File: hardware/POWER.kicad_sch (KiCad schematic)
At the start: 67 parts, among them J4 532610371, SW1 TS-1010-C-A, U1 RT5750A, U13 XC6206P302MR, U2 RT9467, U3 RT4812, U5 RT6150, U6 RT5750A, U7 RT5750A

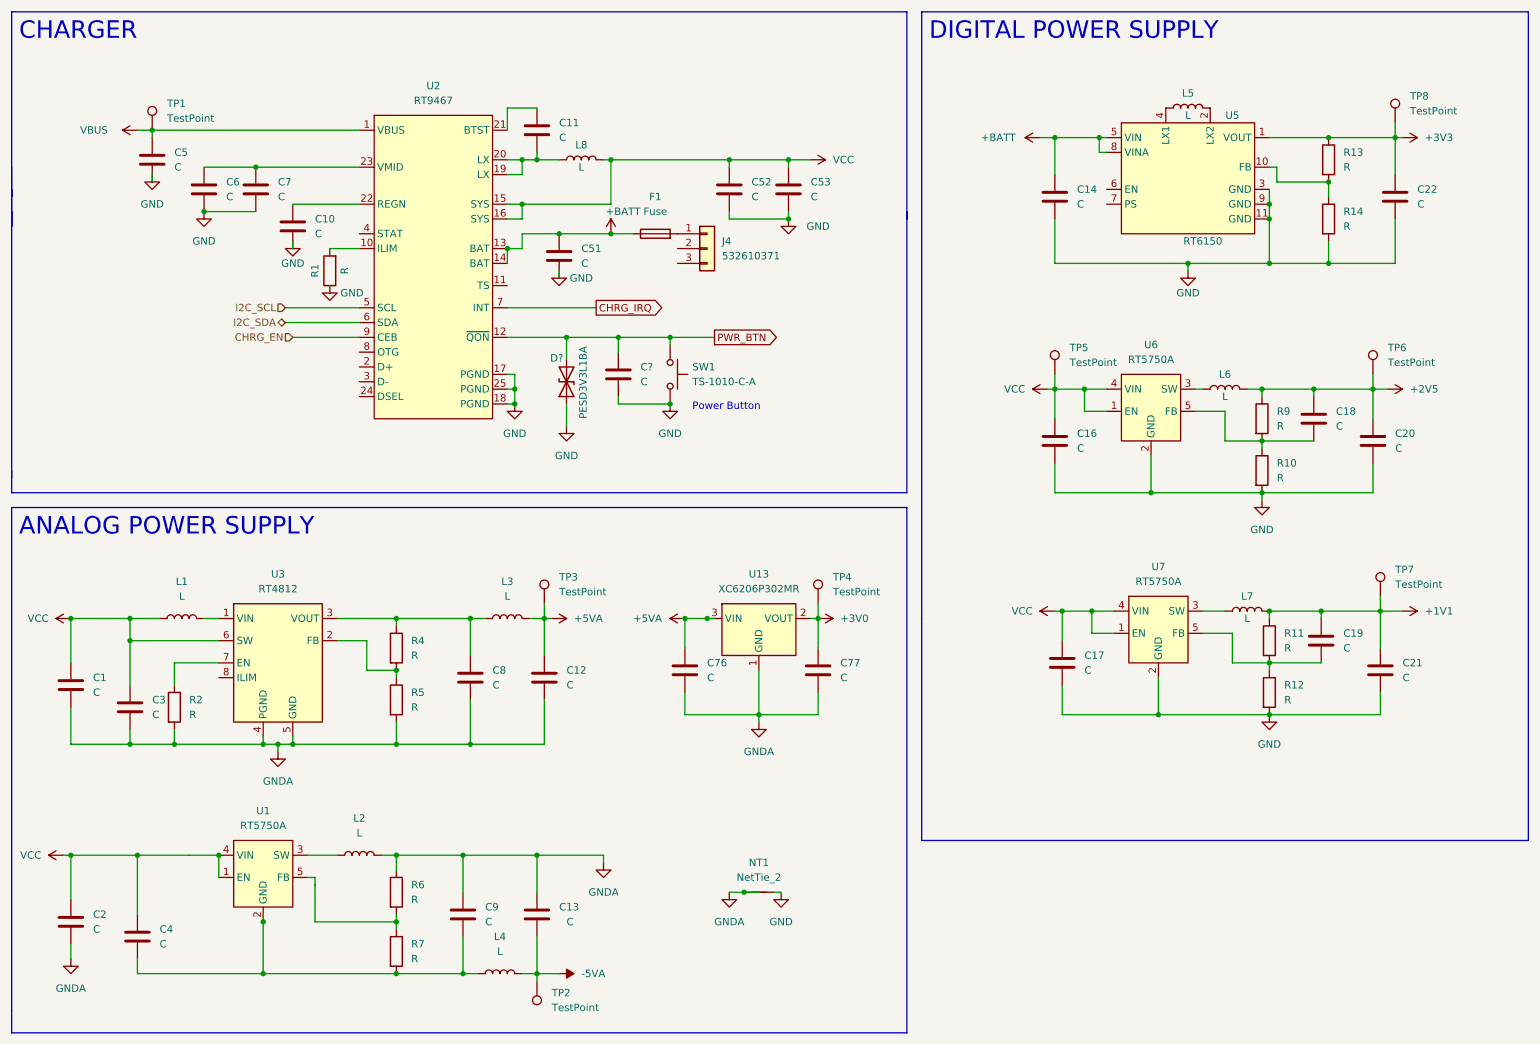
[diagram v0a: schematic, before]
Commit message: replaced dc-dc ics
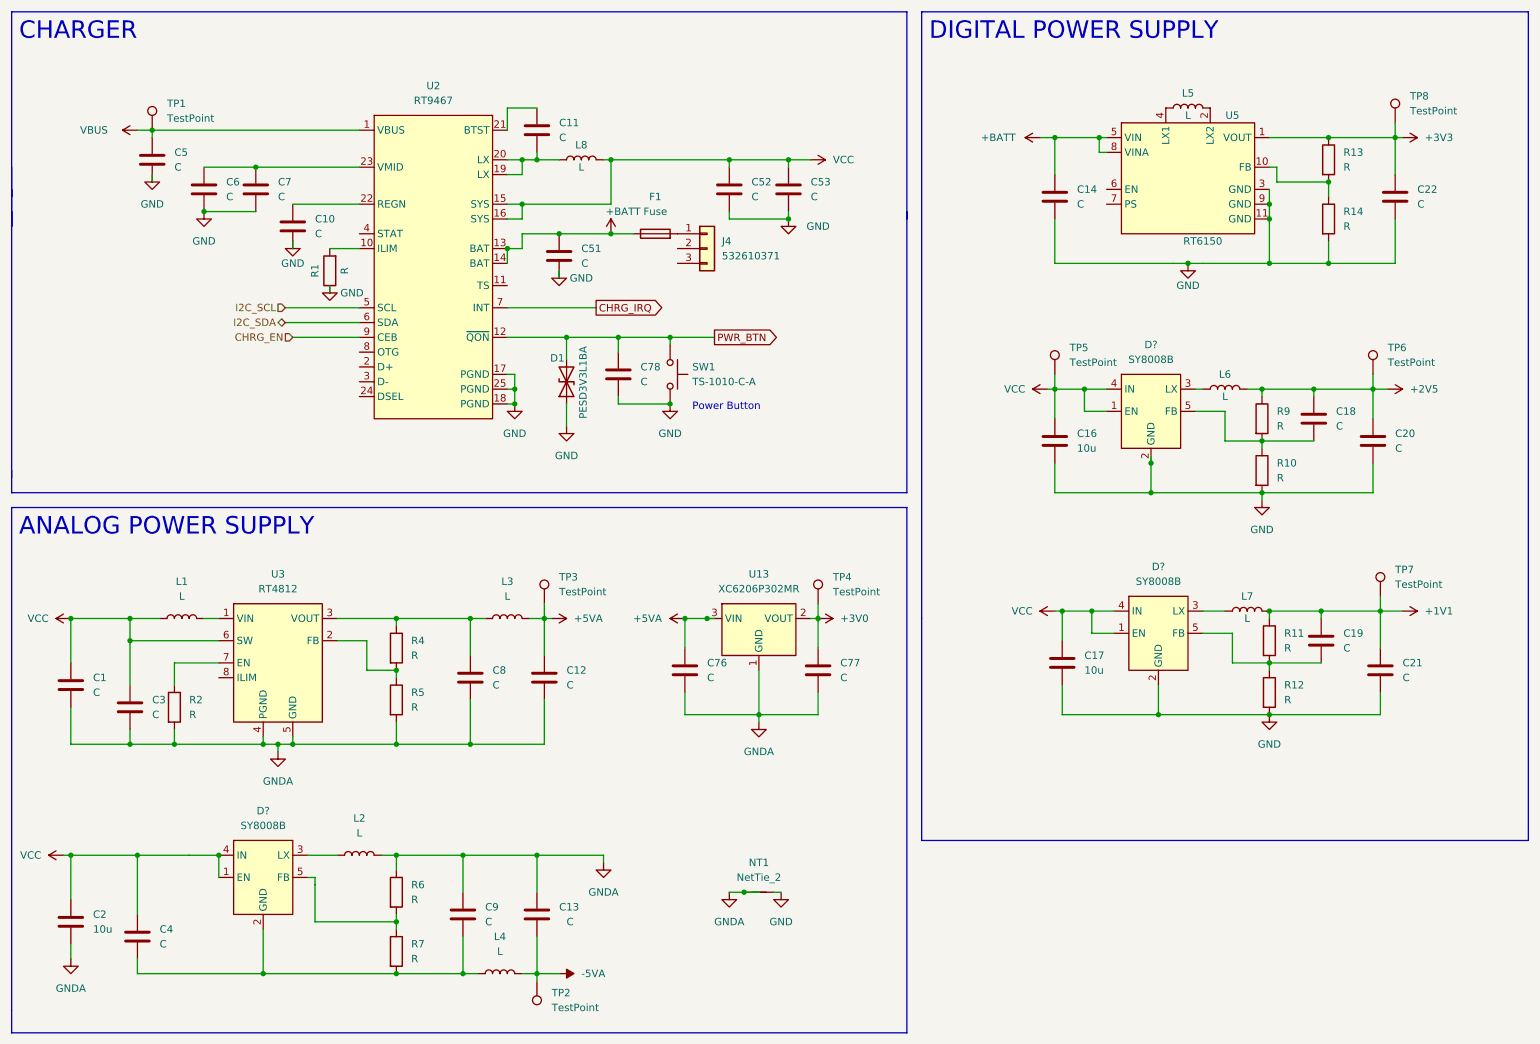
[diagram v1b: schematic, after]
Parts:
- removed U1, U6, U7: RT5750A, rlib_power:SOT-23-5, symbol rlib_power:RT5750A
- added D? (x3): SY8008B, rlib_power:SOT-23-5, symbol rlib_power:SY8008B
- C16, C17, C2: value C -> 10u
- gave numbers to parts that had none: 2
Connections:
- net GND: now also D?.2 (GND), D?.2 (GND)
- net VCC: now also D?.1 (EN), D?.1 (EN), D?.1 (EN), D?.4 (IN), D?.4 (IN), D?.4 (IN)
- net at L2.1: now also D?.3 (LX)
- net at R6.2, R7.1: now also D?.5 (FB)
- net at C4.2, C9.2, L4.1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: now also D?.2 (GND)
- net at C19.2, R11.2, R12.1: now also D?.5 (FB)
- net at L6.1: now also D?.3 (LX)
- net at C18.2, R10.1, R9.2: now also D?.5 (FB)
- net at L7.1: now also D?.3 (LX)

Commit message: sfsf
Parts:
- SW1: footprint rlib_buttons:TS-1010-X-X -> rlib_buttons:GT-TC054A-H035-L1; symbol rlib_buttons:TS-1010-C-A -> rlib_buttons:GT-TC054A-H035-L1
- gave numbers to parts that had none: 3
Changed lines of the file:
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@@
   (symbol (lib_id "rlib_power:SY8008B") (at 214.63 88.9 0) (unit 1)
     (in_bom yes) (on_board yes) (fields_autoplaced)
-    (property "Reference" "D?" (id 0) (at 214.63 77.47 0))
+    (property "Reference" "D12" (id 0) (at 214.63 77.47 0))
     (property "Value" "SY8008B" (id 1) (at 214.63 80.01 0))
     (property "Footprint" "rlib_power:SOT-23-5" (id 2) (at 226.06 81.28 0)
@@
   (symbol (lib_id "rlib_power:SY8008B") (at 215.9 127 0) (unit 1)
     (in_bom yes) (on_board yes) (fields_autoplaced)
-    (property "Reference" "D?" (id 0) (at 215.9 115.57 0))
+    (property "Reference" "D13" (id 0) (at 215.9 115.57 0))
     (property "Value" "SY8008B" (id 1) (at 215.9 118.11 0))
     (property "Footprint" "rlib_power:SOT-23-5" (id 2) (at 227.33 119.38 0)
@@
     (pin "1")
   )
-  (symbol (lib_id "rlib_buttons:TS-1010-C-A") (at 132.08 82.55 270) (unit 1)
+  (symbol (lib_id "rlib_buttons:GT-TC054A-H035-L1") (at 132.08 82.55 270) (unit 1)
     (in_bom yes) (on_board yes) (fields_autoplaced)
     (property "Reference" "SW1" (id 0) (at 135.89 81.2799 90)
@@
       (effects (font (size 1.27 1.27)) (justify left))
     )
-    (property "Footprint" "rlib_buttons:TS-1010-X-X" (id 2) (at 127 81.28 0)
+    (property "Footprint" "rlib_buttons:GT-TC054A-H035-L1" (id 2) (at 127 81.28 0)
       (effects (font (size 1.27 1.27)) hide)
     )
@@
   (symbol (lib_id "rlib_power:SY8008B") (at 62.23 168.91 0) (unit 1)
     (in_bom yes) (on_board yes) (fields_autoplaced)
-    (property "Reference" "D?" (id 0) (at 62.23 157.48 0))
+    (property "Reference" "D11" (id 0) (at 62.23 157.48 0))
     (property "Value" "SY8008B" (id 1) (at 62.23 160.02 0))
     (property "Footprint" "rlib_power:SOT-23-5" (id 2) (at 73.66 161.29 0)

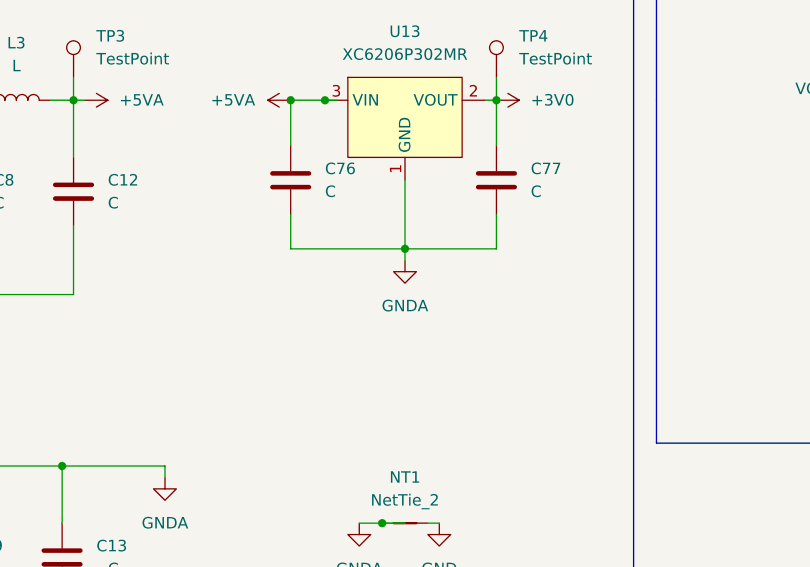
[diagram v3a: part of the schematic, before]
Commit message: added new power list
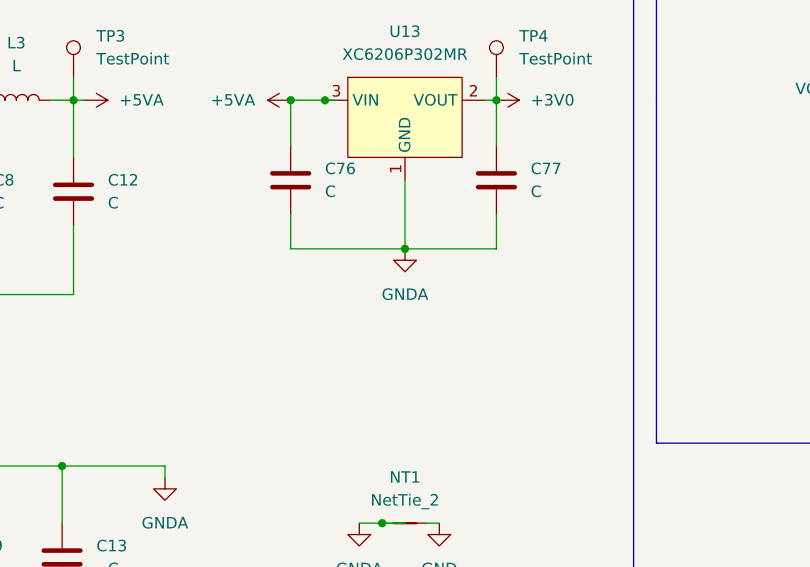
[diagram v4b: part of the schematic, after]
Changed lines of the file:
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@@
     (stroke (width 0) (type default) (color 0 0 0 1))
-  )
-  (wire (pts (xy 147.32 140.97) (xy 147.32 142.24))
-    (stroke (width 0) (type default) (color 0 0 0 0))
   )
   (wire (pts (xy 254 120.65) (xy 254 123.19))
@@
     (pin "5")
   )
-  (symbol (lib_id "power:GNDA") (at 147.32 142.24 0) (unit 1)
-    (in_bom yes) (on_board yes) (fields_autoplaced)
-    (property "Reference" "#PWR0198" (id 0) (at 147.32 148.59 0)
-      (effects (font (size 1.27 1.27)) hide)
-    )
-    (property "Value" "GNDA" (id 1) (at 147.32 147.32 0))
-    (property "Footprint" "" (id 2) (at 147.32 142.24 0)
-      (effects (font (size 1.27 1.27)) hide)
-    )
-    (property "Datasheet" "" (id 3) (at 147.32 142.24 0)
-      (effects (font (size 1.27 1.27)) hide)
-    )
+  (symbol (lib_id "power:GNDA") (at 147.32 140.97 0) (unit 1)
+    (in_bom yes) (on_board yes) (fields_autoplaced)
+    (property "Reference" "#PWR0198" (id 0) (at 147.32 147.32 0)
+      (effects (font (size 1.27 1.27)) hide)
+    )
+    (property "Value" "GNDA" (id 1) (at 147.32 146.05 0))
+    (property "Footprint" "" (id 2) (at 147.32 140.97 0)
+      (effects (font (size 1.27 1.27)) hide)
+    )
+    (property "Datasheet" "" (id 3) (at 147.32 140.97 0)
+      (effects (font (size 1.27 1.27)) hide)
+    )

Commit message: some changes
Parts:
- L1, L2, L3, L4, L5, L6, L7, L8: footprint (none) -> rlib_passive:INDC2520X120N
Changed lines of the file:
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@@
     (property "Reference" "L2" (id 0) (at 78.74 158.75 90))
     (property "Value" "L" (id 1) (at 78.74 161.29 90))
-    (property "Footprint" "" (id 2) (at 78.74 165.1 0)
+    (property "Footprint" "rlib_passive:INDC2520X120N" (id 2) (at 78.74 165.1 0)
       (effects (font (size 1.27 1.27)) hide)
     )
@@
     (property "Reference" "L1" (id 0) (at 48.26 118.11 90))
     (property "Value" "L" (id 1) (at 48.26 120.65 90))
-    (property "Footprint" "" (id 2) (at 48.26 124.46 0)
+    (property "Footprint" "rlib_passive:INDC2520X120N" (id 2) (at 48.26 124.46 0)
       (effects (font (size 1.27 1.27)) hide)
     )
@@
     (property "Reference" "L3" (id 0) (at 104.14 118.11 90))
     (property "Value" "L" (id 1) (at 104.14 120.65 90))
-    (property "Footprint" "" (id 2) (at 104.14 124.46 0)
+    (property "Footprint" "rlib_passive:INDC2520X120N" (id 2) (at 104.14 124.46 0)
       (effects (font (size 1.27 1.27)) hide)
     )
@@
     (property "Reference" "L4" (id 0) (at 102.87 179.07 90))
     (property "Value" "L" (id 1) (at 102.87 181.61 90))
-    (property "Footprint" "" (id 2) (at 102.87 185.42 0)
+    (property "Footprint" "rlib_passive:INDC2520X120N" (id 2) (at 102.87 185.42 0)
       (effects (font (size 1.27 1.27)) hide)
     )
@@
     (property "Reference" "L6" (id 0) (at 227.33 82.55 90))
     (property "Value" "L" (id 1) (at 227.33 86.36 90))
-    (property "Footprint" "" (id 2) (at 227.33 85.09 0)
+    (property "Footprint" "rlib_passive:INDC2520X120N" (id 2) (at 227.33 85.09 0)
       (effects (font (size 1.27 1.27)) hide)
     )
@@
     (property "Reference" "L5" (id 0) (at 220.98 34.29 90))
     (property "Value" "L" (id 1) (at 220.98 38.1 90))
-    (property "Footprint" "" (id 2) (at 220.98 36.83 0)
+    (property "Footprint" "rlib_passive:INDC2520X120N" (id 2) (at 220.98 36.83 0)
       (effects (font (size 1.27 1.27)) hide)
     )
@@
     (property "Reference" "L8" (id 0) (at 116.84 43.18 90))
     (property "Value" "L" (id 1) (at 116.84 46.99 90))
-    (property "Footprint" "" (id 2) (at 116.84 45.72 0)
+    (property "Footprint" "rlib_passive:INDC2520X120N" (id 2) (at 116.84 45.72 0)
       (effects (font (size 1.27 1.27)) hide)
     )
@@
     (property "Reference" "L7" (id 0) (at 231.14 120.65 90))
     (property "Value" "L" (id 1) (at 231.14 124.46 90))
-    (property "Footprint" "" (id 2) (at 231.14 123.19 0)
-      (effects (font (size 1.27 1.27)) hide)
-    )
+    (property "Footprint" "rlib_passive:INDC2520X120N" (id 2) (at 231.14 123.19 0)
+      (effects (font (size 1.27 1.27)) hide)
+    )
